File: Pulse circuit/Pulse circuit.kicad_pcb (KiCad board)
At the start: 4 copper layers, 76.9 x 88 mm, 9 parts, among them J1 Conn_01x02_Pin, U1 module_max30102, U2 module_max30102, U3 DOIT-ESP32-DEVKIT-V1

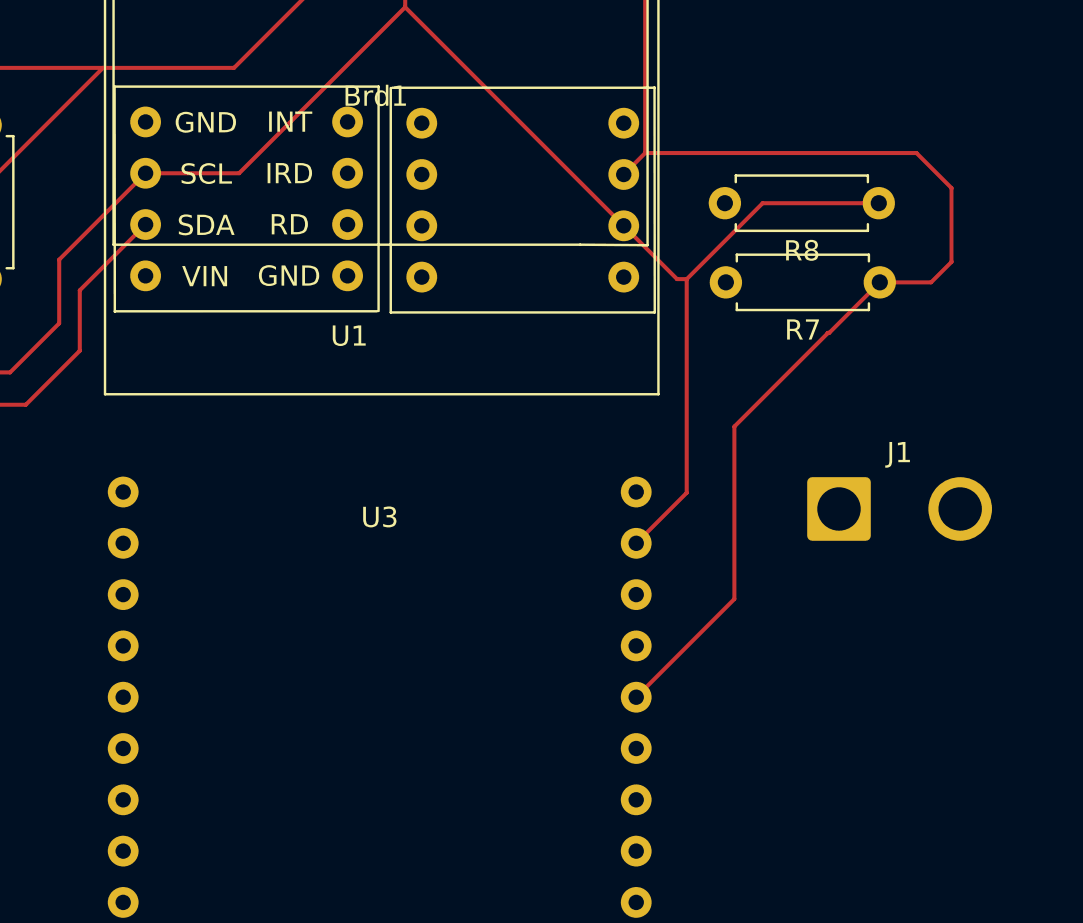
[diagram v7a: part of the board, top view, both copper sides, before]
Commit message: new routes for PCB
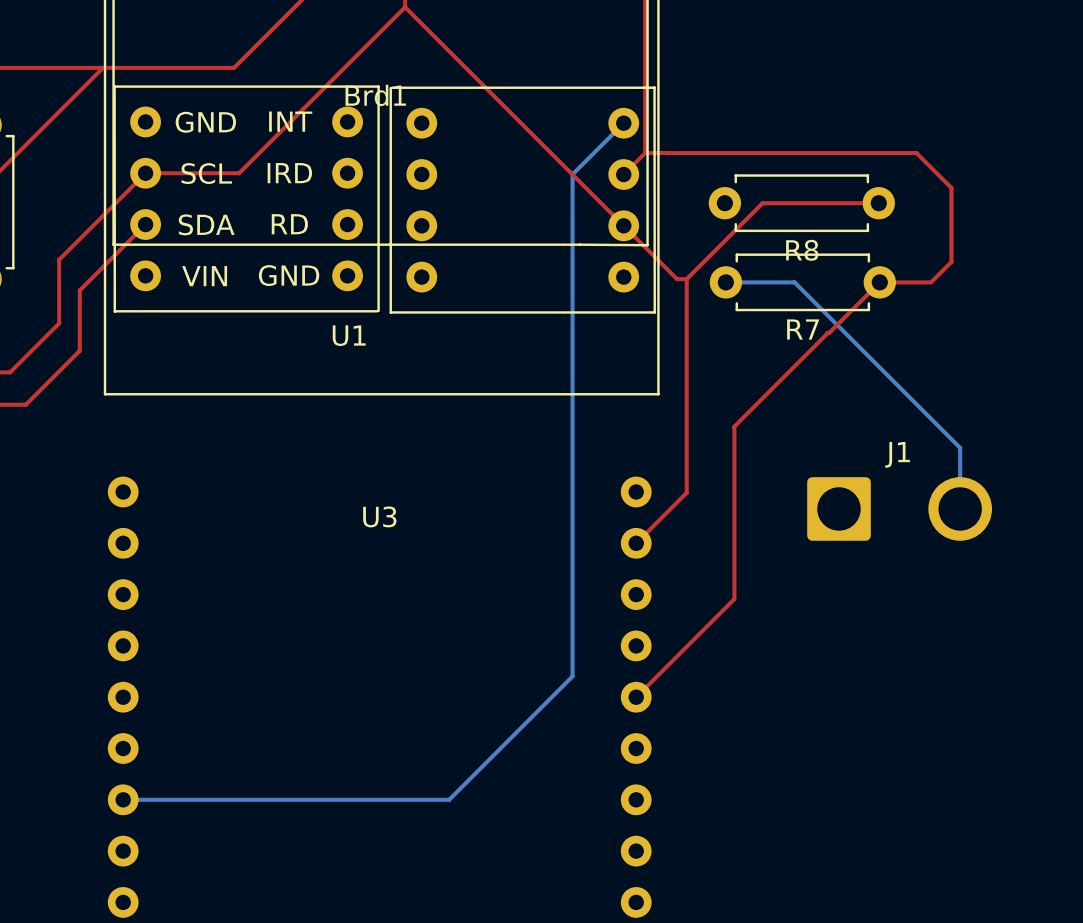
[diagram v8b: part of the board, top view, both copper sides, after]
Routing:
- net INT5v: track 0.00 -> 53.2 mm
- net 5V: track 73.2 -> 91.2 mm
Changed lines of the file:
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@@
+	)
+	(segment
+		(start 180.69 77.69)
+		(end 172.49 69.49)
+		(width 0.2)
+		(layer "B.Cu")
+		(net 5)
+	)
+	(segment
+		(start 180.69 80.71)
+		(end 180.69 77.69)
+		(width 0.2)
+		(layer "B.Cu")
+		(net 5)
+	)
+	(segment
+		(start 172.49 69.49)
+		(end 169.09 69.49)
+		(width 0.2)
+		(layer "B.Cu")
+		(net 5)
 	)
 	(segment
@@
 	)
 	(segment
+		(start 161.5 64.1425)
+		(end 161.5 89)
+		(width 0.2)
+		(layer "B.Cu")
+		(net 10)
+	)
+	(segment
+		(start 155.39 95.11)
+		(end 139.25 95.11)
+		(width 0.2)
+		(layer "B.Cu")
+		(net 10)
+	)
+	(segment
+		(start 161.5 89)
+		(end 155.39 95.11)
+		(width 0.2)
+		(layer "B.Cu")
+		(net 10)
+	)
+	(segment
+		(start 164.0325 61.61)
+		(end 161.5 64.1425)
+		(width 0.2)
+		(layer "B.Cu")
+		(net 10)
+	)
+	(segment
